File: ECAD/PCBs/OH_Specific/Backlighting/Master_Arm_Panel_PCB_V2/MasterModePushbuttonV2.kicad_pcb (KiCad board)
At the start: 2 copper layers, 45.7 x 123.5 mm, 61 parts, among them J1 Conn_01x02_Female, J10 Conn_01x04_Female, J2 Conn_01x02_Female, J9 Conn_01x04_Female, SW1 PT_Tactile_Switch_Led, SW2 PT_Tactile_Switch_Led, SW3 PT_Tactile_Switch_Led

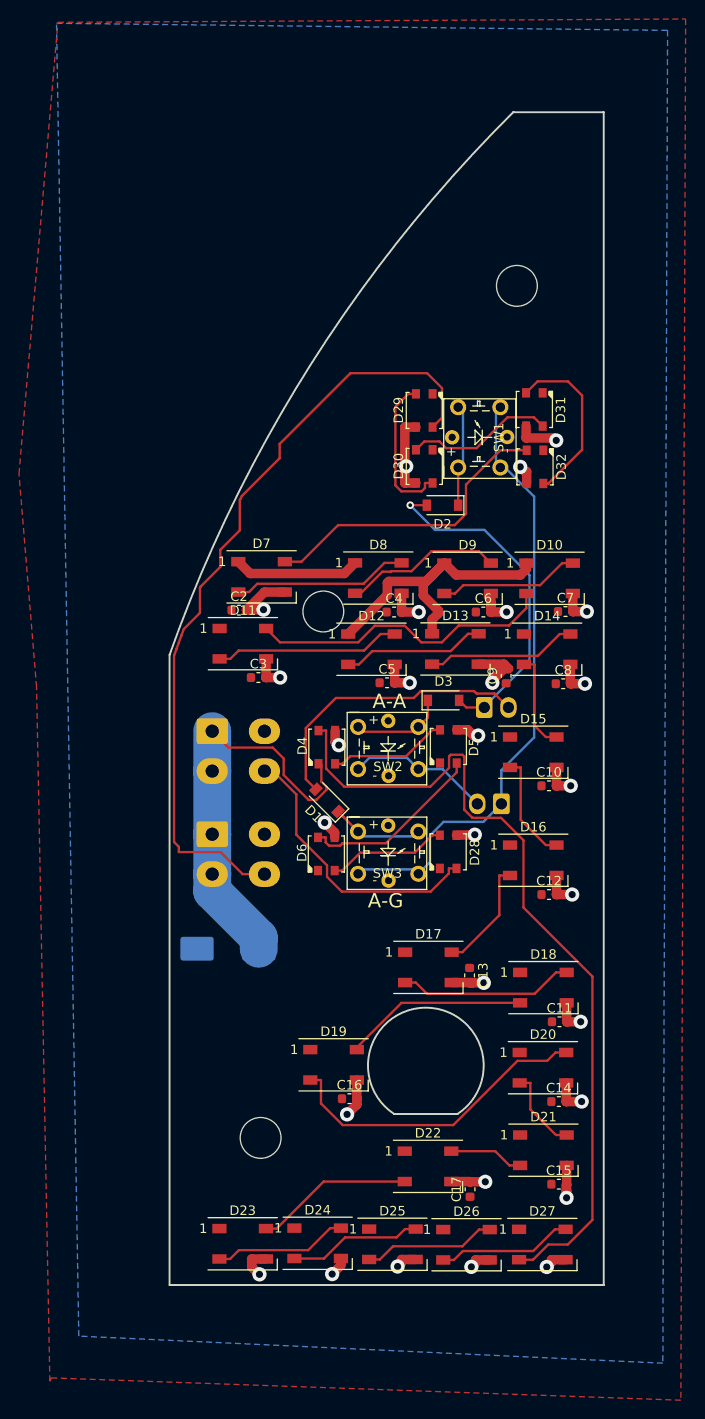
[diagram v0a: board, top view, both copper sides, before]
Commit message: Backlighting PCB Updates
Added - Master mode button mounting holes to Master Arm panel
Added - ECM Jett button mounting holes to ECM JETT panel.
Added - Silkscreens to VID RCD PCB
Added - Ready LED to VID RCD PCB
Added - Manufacturing files for VID RCD PCB
Added - Manufacturing files for SPIN RCVY PCB
Added - Manufacturing files for MASTER ARM PCB
Added - Manufacturing files for ECM JETT PCB
Added - Manufacturing files for HUD PCB
Added - Manufacturing files for DEFOG LEVER PCB
Added - Manufacturing files for AV COOL PCB
Added - Manufacturing files for LDG WING FOLD PCB
Added - Extra backlighting string port to power distro PCB
Added - External power input connector to power distro PCB if ATX PSU cannot provide enough 5V current.
Added - Fan voltage selector on power distro PCB
Changed - Power distro PCB is now a solid copper fill on both sides to improve voltage drop under load.
Changed - VID RCD panel connectors to mini-fit
Changed - VID RCD panel LED pads from solid to thermal relief.
Changed - ECM JETT panel LED pads from solid to thermal relief.
Changed - MASTER ARM panel LED pads from solid to thermal relief.
Changed - SPIN RCVY panel LED pads from solid to thermal relief.
Changed - INTR LT panel LED pads from solid to thermal relief.
Changed - AV COOL panel LED pads from solid to thermal relief.
Changed - LDG WING FOLD panel LED pads from solid to thermal relief.
Changed - HUD panel LED pads from solid to thermal relief.
Changed - HUD panel connectors to mini-fit
Changed - JETT STATION SELECT PLACARD PCB connector to mini-fit
Fixed - Fan headers on power distro PCB mis-wired.
Removed - 1 row of LEDs on DEFOG PCB to improve reparability.
Removed - Version 1 folder from repo when it is replaced with a version 2 folder.
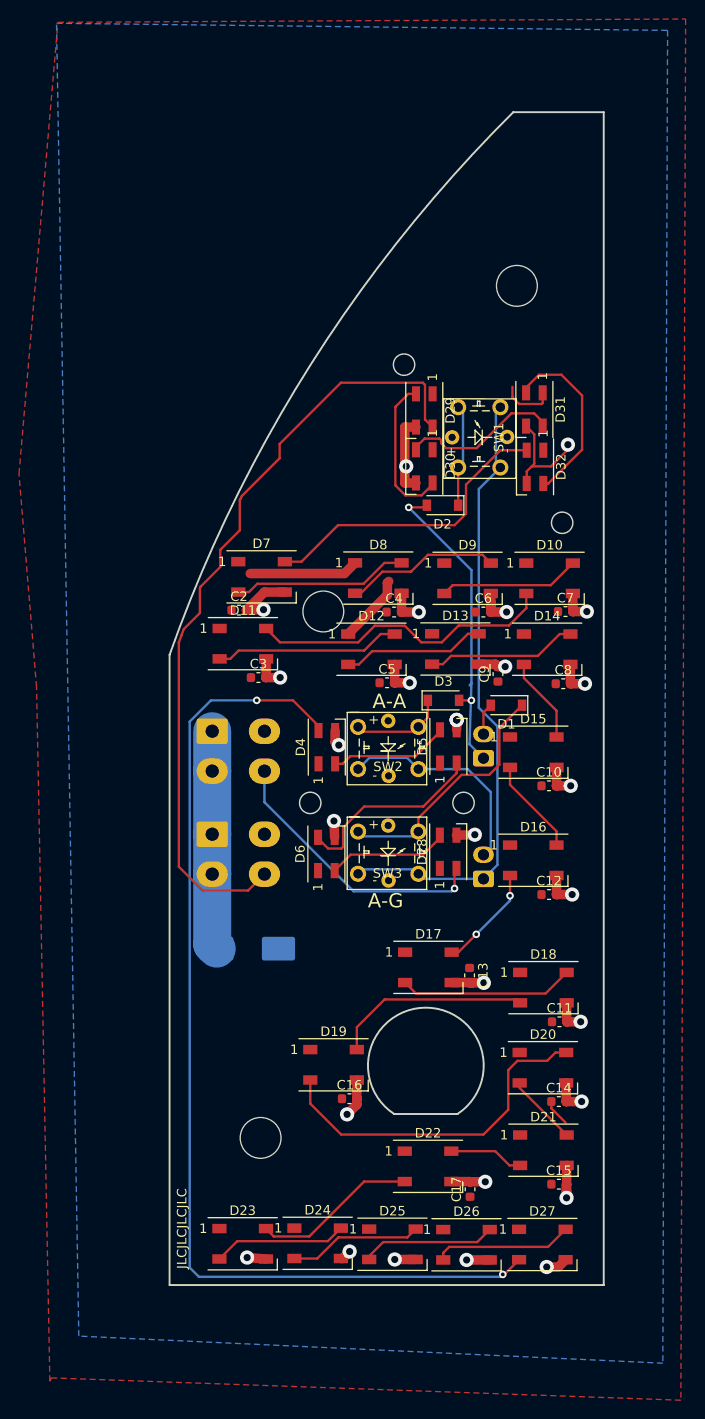
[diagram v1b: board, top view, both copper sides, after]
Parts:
- added G***: LOGO, OH_General:CC-BY-NC-SA-Small, B.Cu at (223.0, 70.4)
- D28, D29, D30, D31, D32, D4, D5, D6: footprint WS2812B:LED3535 -> LED_SMD:LED_SK6812MINI_PLCC4_3.5x3.5mm_P1.75mm
- moved D1 21.4 mm to (233.8, 91.5), turned to 180 degrees
- moved J2 8.12 mm to (231.4, 109.8), turned to 90 degrees
- moved J1 5.35 mm to (231.4, 97.1), turned to 90 degrees
- moved C1 2.07 mm to (206.5, 117.1), turned to 0 degrees
- moved C9 0.88 mm to (232.9, 88.2)
- renumbered G*** to G1
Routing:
- net /LED+5V: track 91.2 -> 50.4 mm
- net /Column2: track 30.6 -> 3.36 mm
- net Net-(D27-Pad2): track 87.9 -> 109.4 mm, vias 0 -> 2
- net Net-(D1-Pad1): track 9.76 -> 26.3 mm
- net /Row2: track 15.1 -> 22.9 mm
- net Net-(D19-Pad2): track 33.5 -> 36.8 mm
- net /Column1: track 36.2 -> 33.8 mm, vias 1 -> 2
- net Net-(D18-Pad2): track 19.4 -> 20.9 mm
- net Net-(D20-Pad2): track 8.86 -> 7.54 mm
- net Net-(D15-Pad2): track 11.5 -> 10.2 mm
- net Net-(D14-Pad2): track 10.4 -> 9.07 mm
- net Net-(D5-Pad2): track 19.4 -> 20.7 mm
- net /LEDGND: track 100.4 -> 99.2 mm
- net Net-(D30-Pad2): track 15.7 -> 16.9 mm
- net Net-(D16-Pad2): track 11.9 -> 11.0 mm, vias 0 -> 2
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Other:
- outline, holes or cut-outs redrawn
- board text added: "C1"
- board text added: "C2"
- board text added: "JLCJLCJLCJLC"
- board text added: "MASTER ARM Panel Backlight Designed by L. Walker"
- board text added: "R1"
- board text added: "R2"
- board text added: "SWITCH COL"
- board text added: "Version 2.1"
- board text removed: "Compatible with"
- board text removed: "F/A 18C Simulator MASTER ARM Panel Backlight Designed & Assembled in Australia L. Walker 2021"
- board text removed: "SW COL"
- board text removed: "Version 2.0"

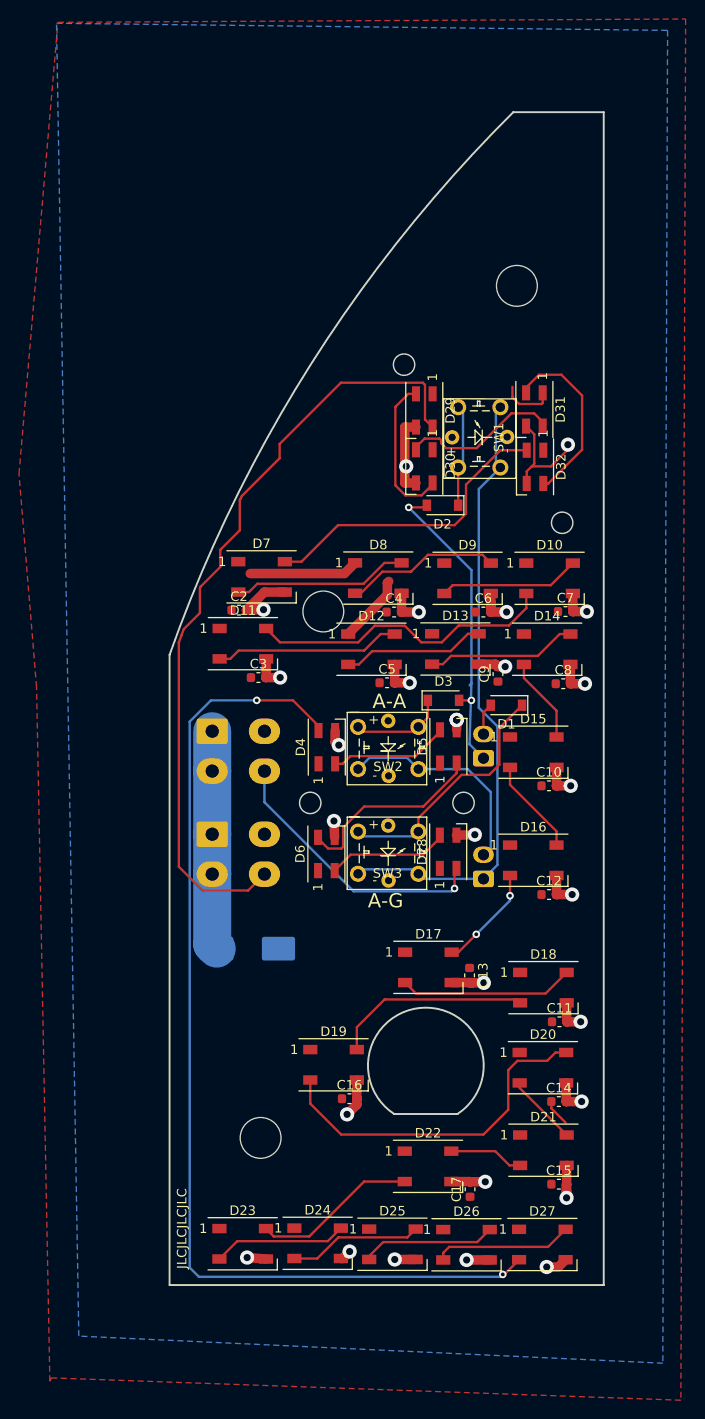
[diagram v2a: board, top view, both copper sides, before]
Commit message: Master Arm and Defog Lever PCB Bugfixes
Increased space between the 3535 pixel traces to cater for JLCPCB manufacturing tolerances. The current design shorted tracks that went between pads on the short edge of 3535 pixels to one of the pads.
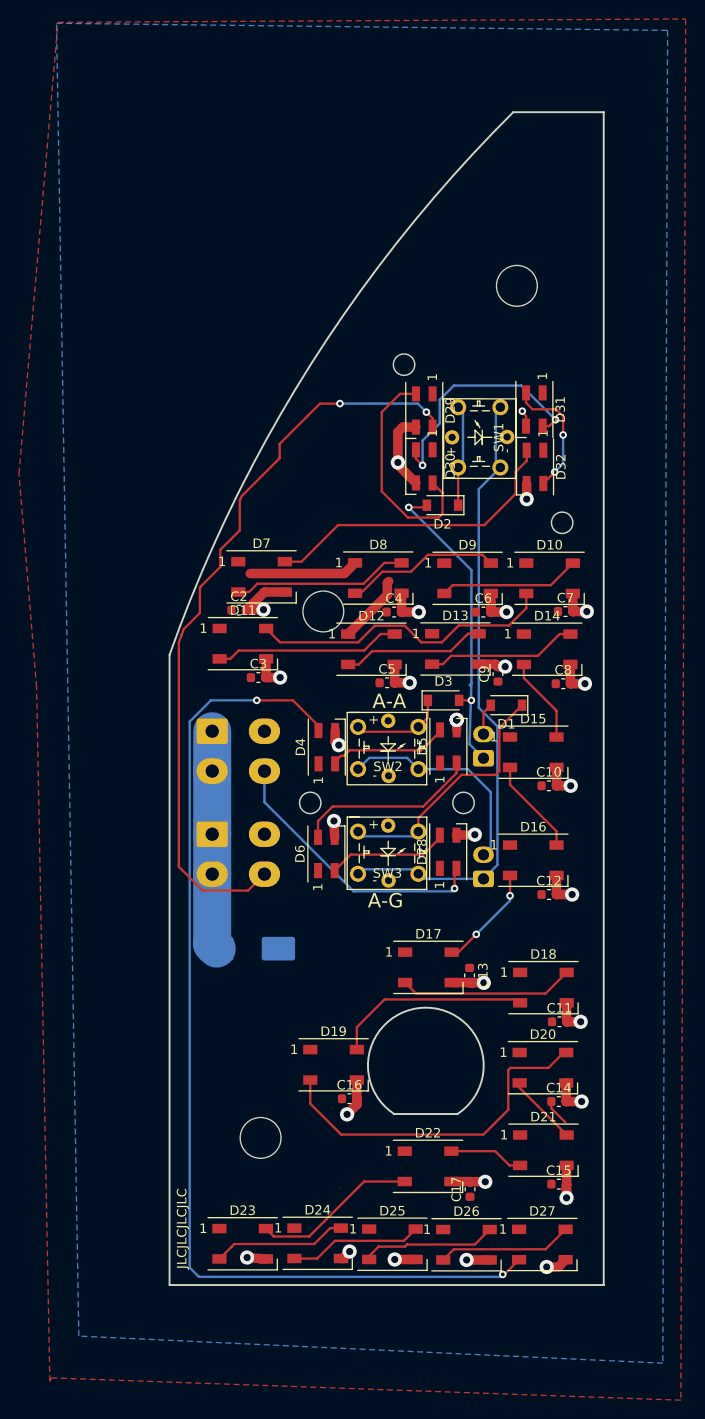
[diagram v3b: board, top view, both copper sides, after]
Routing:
- net Net-(D30-Pad2): track 16.9 -> 25.5 mm, vias 0 -> 2
- net /LEDGND: track 99.2 -> 90.7 mm, vias 28 -> 29
- net Net-(D29-Pad2): track 16.0 -> 24.1 mm
- net Net-(D31-Pad2): track 19.2 -> 13.5 mm, vias 0 -> 2
- net /LED+5V: track 50.4 -> 44.7 mm
- net /DATAIN: track 82.4 -> 78.9 mm, vias 0 -> 2
- net Net-(D5-Pad2): track 20.7 -> 19.5 mm

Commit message: Master Arm Update
Updated switch actuators and inserted new Master Mode PCB. Converted LEDs around indicator buttons to 2020 RGB and switches to Omron B3F-1026 tactiles to reduce footprint and increase the margins for the light path to the legends.
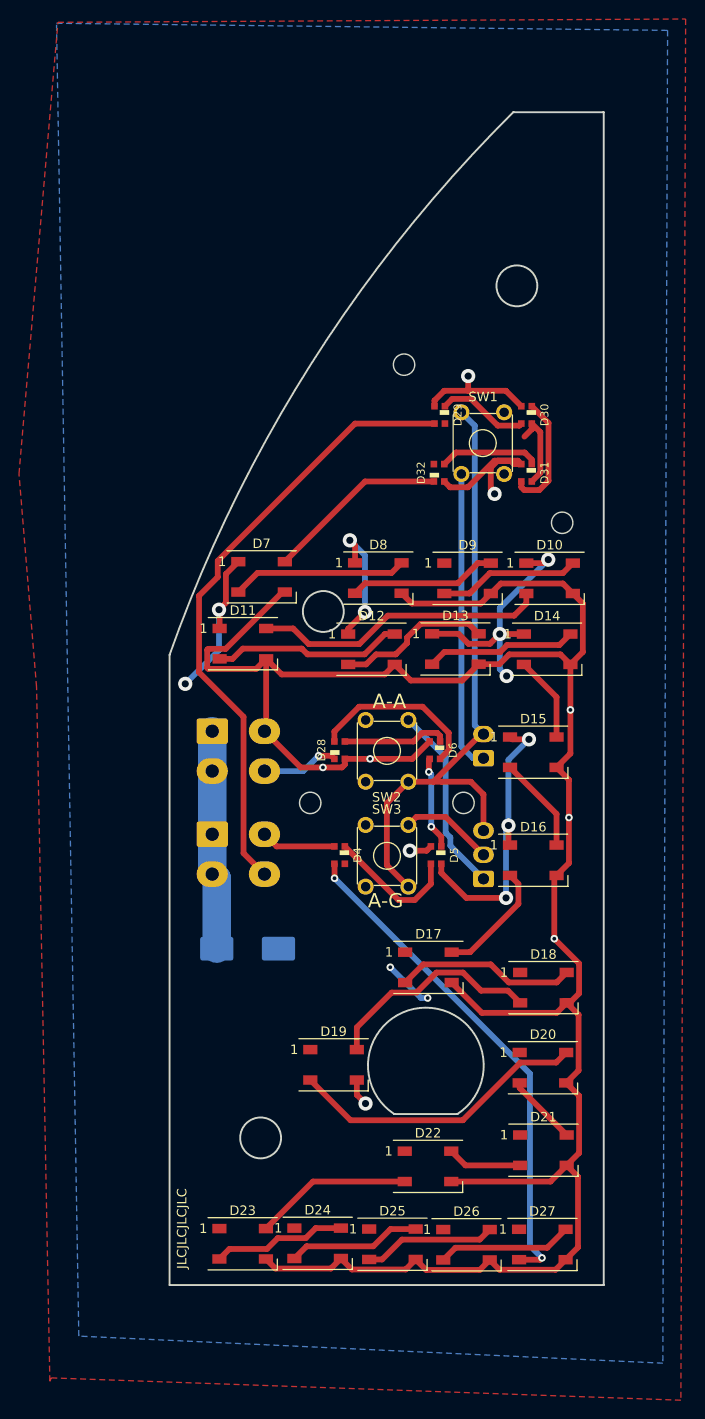
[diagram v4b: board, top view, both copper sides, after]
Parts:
- removed 1, 2, 3: OH_Panel_Fastner_Keepout, OH_Backlighting:OH_Panel_6-32_PHS
- removed C10, C11, C12, C13, C14, C15, C16, C17, C2, C3, C4, C5, C6, C7, C8, C9: C, Capacitor_SMD:C_0603_1608Metric
- removed D1, D2, D3: D, Diode_SMD:D_SOD-123
- removed G***: LOGO, OH_General:CC-BY-NC-SA-Small
- removed G***: LOGO, OH_General:OH_LOGO_37.7mm_5.9mm
- removed G1: LOGO, Kicad Footprint Files:S2ALToggle
- D28, D29, D30, D31, D32, D4, D5, D6: value WS2812B -> WS2812B-2020; footprint LED_SMD:LED_SK6812MINI_PLCC4_3.5x3.5mm_P1.75mm -> KiCAD Libraries:WS2812-2020
- J1: renamed from J9; value Conn_01x04_Female -> BL IN
- J2: renamed from J10; value Conn_01x04_Female -> BL OUT
- J3: renamed from J1; value Conn_01x02_Female -> READY
- J4: renamed from J2; value Conn_01x02_Female -> MASTER MODE; footprint Connector_Molex:Molex_KK-254_AE-6410-02A_1x02_P2.54mm_Vertical -> Connector_Molex:Molex_KK-254_AE-6410-03A_1x03_P2.54mm_Vertical
- SW1: value PT_Tactile_Switch_Led -> READY; footprint PT_Library_v001:PT_Small_Tactile_Switch_With_LED -> Button_Switch_THT:SW_TH_Tactile_Omron_B3F-10xx
- SW2: value PT_Tactile_Switch_Led -> A/A; footprint PT_Library_v001:PT_Small_Tactile_Switch_With_LED -> Button_Switch_THT:SW_TH_Tactile_Omron_B3F-10xx
- SW3: value PT_Tactile_Switch_Led -> A/G; footprint PT_Library_v001:PT_Small_Tactile_Switch_With_LED -> Button_Switch_THT:SW_TH_Tactile_Omron_B3F-10xx
- moved D6 15.8 mm to (226.2, 96.2)
- moved D28 15.7 mm to (216.2, 96.2), turned to 270 degrees
- moved D30 12.1 mm to (235.9, 60.9), turned to 90 degrees
- moved D5 11.5 mm to (226.4, 107.3)
- moved D4 11.4 mm to (216.2, 107.3)
- moved D32 10.1 mm to (226.7, 67.0)
- moved D31 6.72 mm to (235.9, 67.0), turned to 90 degrees
- moved SW1 4.32 mm to (229.0, 67.2)
- moved SW2 3.68 mm to (223.4, 93.1), turned to 270 degrees
- moved SW3 3.66 mm to (223.4, 104.1), turned to 270 degrees
- moved D29 1.69 mm to (226.8, 60.9), turned to 90 degrees
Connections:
- D28 pad 1: /LED+5V -> /DATAOUT
- D28 pad 2: /DATAOUT -> /LEDGND
- D28 pad 3: /LEDGND -> Net-(D28-Pad3)
- D28 pad 4: Net-(D28-Pad4) -> /LED+5V
- D29 pad 1: /LED+5V -> Net-(D29-Pad1)
- D29 pad 2: Net-(D29-Pad2) -> /LEDGND
- D29 pad 3: /LEDGND -> /DATAIN
- D29 pad 4: /DATAIN -> /LED+5V
- D30 pad 1: /LED+5V -> Net-(D30-Pad1)
- D30 pad 2: Net-(D30-Pad2) -> /LEDGND
- D30 pad 3: /LEDGND -> Net-(D29-Pad1)
- D30 pad 4: Net-(D29-Pad2) -> /LED+5V
- D31 pad 1: /LED+5V -> Net-(D31-Pad1)
- D31 pad 2: Net-(D31-Pad2) -> /LEDGND
- D31 pad 3: /LEDGND -> Net-(D30-Pad1)
- D31 pad 4: Net-(D30-Pad2) -> /LED+5V
- D32 pad 1: /LED+5V -> Net-(D32-Pad1)
- D32 pad 2: Net-(D32-Pad2) -> /LEDGND
- D32 pad 3: /LEDGND -> Net-(D31-Pad1)
- D32 pad 4: Net-(D31-Pad2) -> /LED+5V
- D4 pad 1: /LED+5V -> Net-(D4-Pad1)
- D4 pad 2: Net-(D4-Pad2) -> /LEDGND
- D4 pad 3: /LEDGND -> Net-(D27-Pad2)
- D4 pad 4: Net-(D27-Pad2) -> /LED+5V
- D5 pad 1: /LED+5V -> Net-(D5-Pad1)
- D5 pad 2: Net-(D5-Pad2) -> /LEDGND
- D5 pad 3: /LEDGND -> Net-(D4-Pad1)
- D5 pad 4: Net-(D4-Pad2) -> /LED+5V
- D6 pad 1: /LED+5V -> Net-(D28-Pad3)
- D6 pad 2: Net-(D28-Pad4) -> /LEDGND
- D6 pad 3: /LEDGND -> Net-(D5-Pad1)
- D6 pad 4: Net-(D5-Pad2) -> /LED+5V
- D7 pad 4: Net-(D32-Pad2) -> Net-(D32-Pad1)
- J3 pad 1: /Column1 -> /READY_SW
- J3 pad 2: /Column2 -> GND
- J4 pad 1: /Row1 -> /AA_SW
- J4 pad 2: /Row2 -> /AG_SW
- SW1 pad 1: Net-(D2-Pad1) -> /READY_SW
- SW1 pad 2: Net-(D2-Pad1) -> GND
- SW1 pad 3: /Row1 -> (no net)
- SW1 pad 4: /Row1 -> (no net)
- SW2 pad 1: Net-(D3-Pad1) -> /AA_SW
- SW2 pad 2: Net-(D3-Pad1) -> GND
- SW2 pad 3: /Row2 -> (no net)
- SW2 pad 4: /Row2 -> (no net)
- SW3 pad 1: Net-(D1-Pad1) -> /AG_SW
- SW3 pad 2: Net-(D1-Pad1) -> GND
- SW3 pad 3: /Row1 -> (no net)
- SW3 pad 4: /Row1 -> (no net)
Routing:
- net /LEDGND: track 90.7 -> 284.6 mm, vias 29 -> 9
- net /LED+5V: track 44.7 -> 144.8 mm, vias 0 -> 12
- net GND: track 0.00 -> 67.4 mm
- net /Row1: track 66.8 -> 0.00 mm
- net Net-(D27-Pad2): track 109.4 -> 53.0 mm
- net /Column1: track 33.8 -> 0.00 mm, vias 2 -> 0
- net Net-(D32-Pad2): track 32.3 -> 0.00 mm
- net /READY_SW: track 0.00 -> 31.5 mm
- net Net-(D1-Pad1): track 26.7 -> 0.00 mm
- net Net-(D30-Pad2): track 25.5 -> 0.00 mm, vias 2 -> 0
- net Net-(D29-Pad2): track 24.1 -> 0.00 mm
- net /Row2: track 22.9 -> 0.00 mm
- net /DATAOUT: track 29.5 -> 8.17 mm
- net /AA_SW: track 0.00 -> 20.0 mm
- net Net-(D5-Pad2): track 19.5 -> 0.00 mm
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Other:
- outline, holes or cut-outs redrawn
- board text added: "A/A"
- board text added: "A/G"
- board text added: "GND"
- board text added: "MASTER MODE"
- board text added: "RDY"
- board text added: "READY SW"
- board text added: "Version 2.2"
- board text removed: "C1"
- board text removed: "C2"
- board text removed: "R1"
- board text removed: "R2"
- board text removed: "SWITCH COL"
- board text removed: "SWITCH ROW"
- board text removed: "Version 2.1"
